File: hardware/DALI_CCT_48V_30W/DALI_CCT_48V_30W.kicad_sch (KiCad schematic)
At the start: 82 parts, among them J1 Phoenix 5.08mm 2-pin 48V_IN, J2 DALI_A/DALI_B Phoenix 5.08mm, J3 LED+/WW-/CW- Phoenix 5.08mm, J4 SWD 1.27mm 4-pin (GND/SWDIO/S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, Q1 AON7534 N-ch 30V 25A, Q2 AON7534 N-ch 30V 25A, Q3 AON6424 N-ch 40V 20A, Q4 AON6424 N-ch 40V 20A

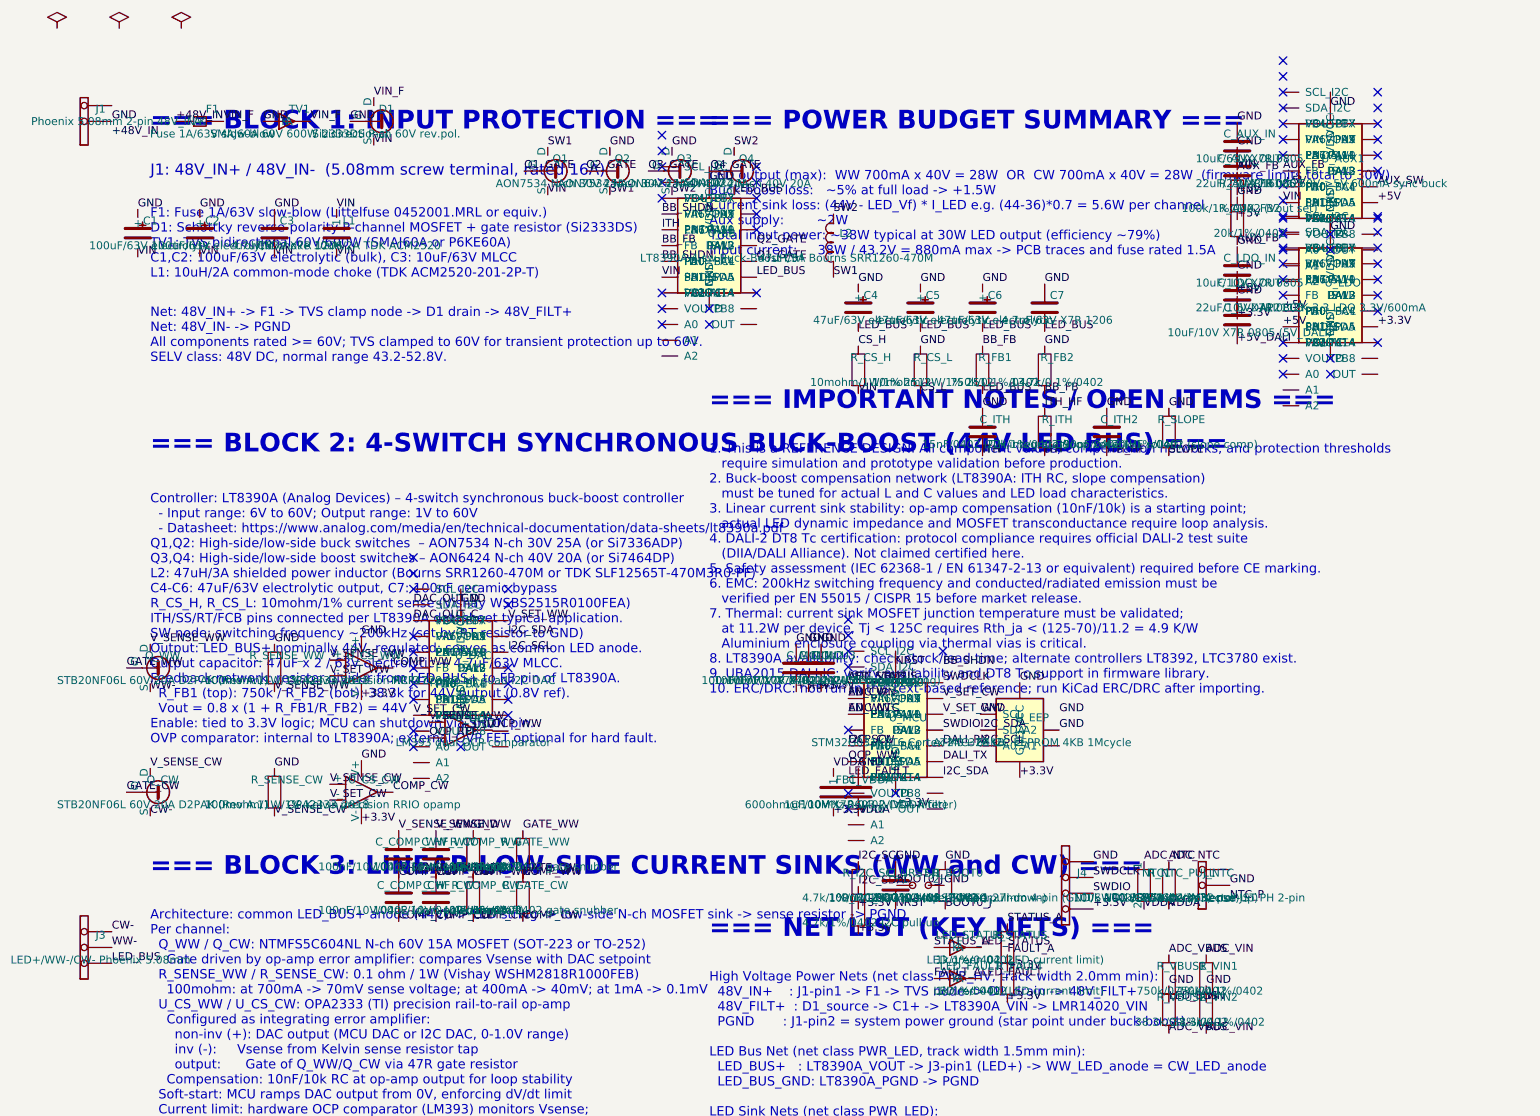
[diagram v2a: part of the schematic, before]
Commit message: Add exact LT8390AIFE KiCad symbol
Co-authored-by: manuelh83 <208121220+manuelh83@users.noreply.github.com>
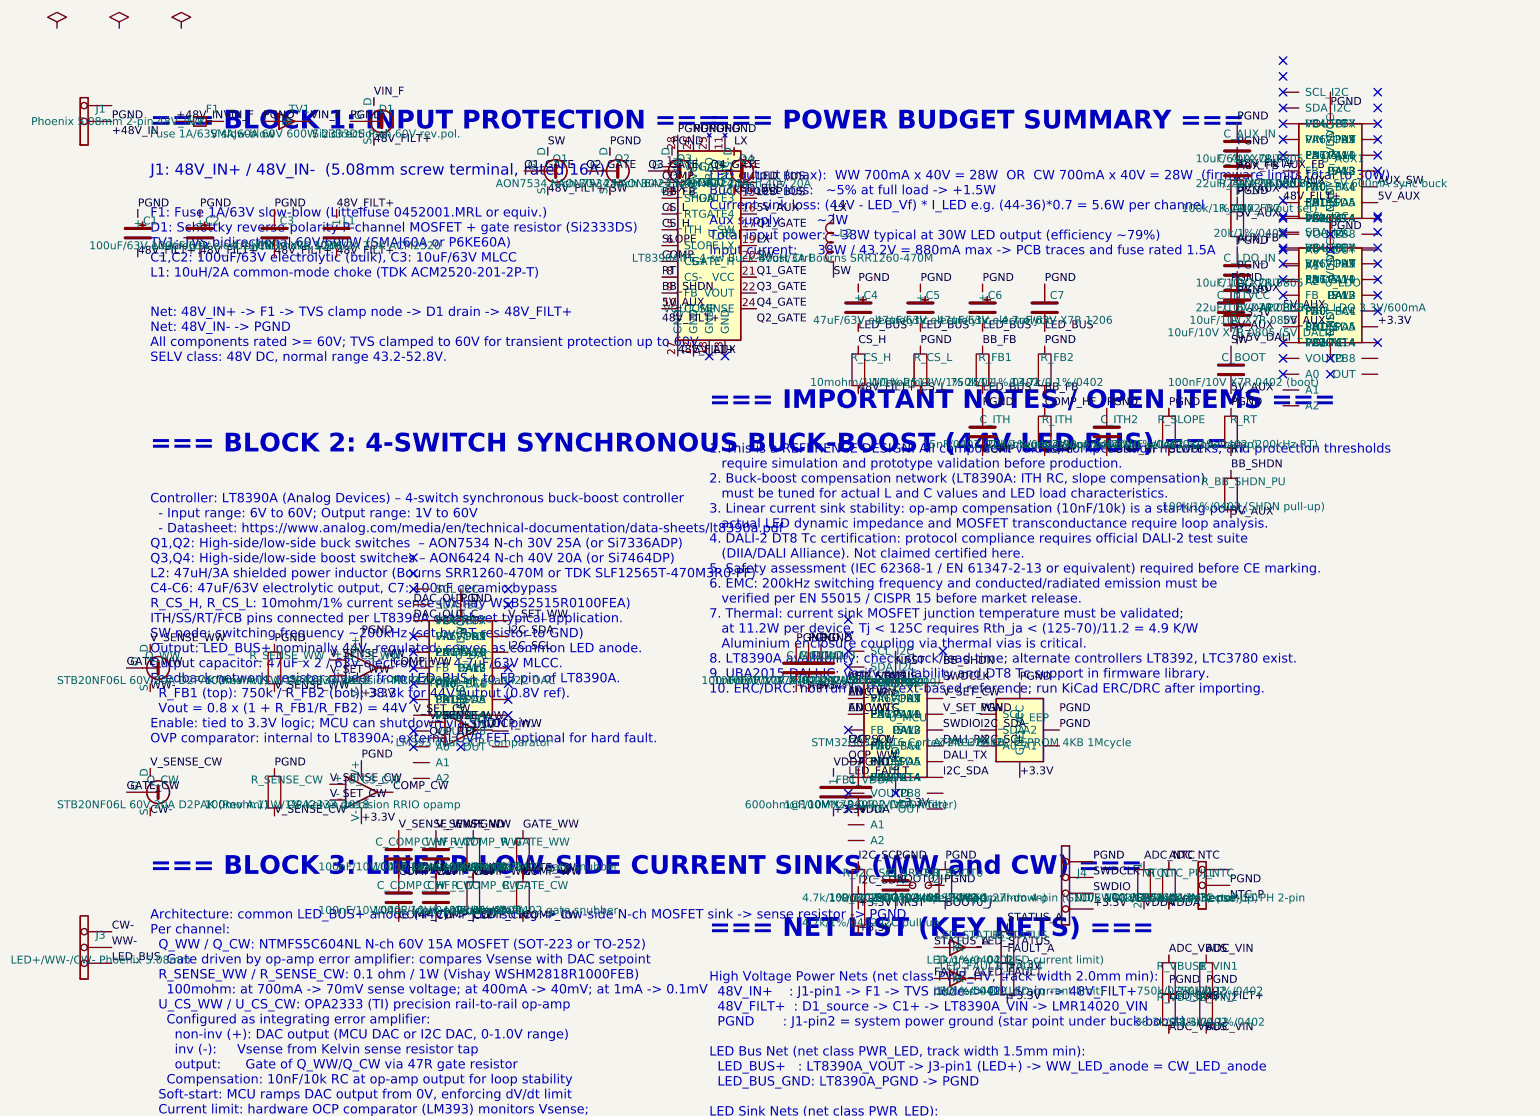
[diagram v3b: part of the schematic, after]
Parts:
- added C_BOOT: 100nF/10V X7R 0402 (boot), Capacitor_SMD:C_0402_1005Metric, symbol Device:C
- added C_INTVCC: 10uF/10V X7R 0805, Capacitor_SMD:C_0805_2012Metric, symbol Device:C
- added R_BB_SHDN_PU: 100k/1%/0402 (SHDN pull-up), Resistor_SMD:R_0402_1005Metric, symbol Device:R
- added R_RT: 470k/1%/0402 (200kHz RT), Resistor_SMD:R_0402_1005Metric, symbol Device:R
- U_BB: value LT8390A 4-sw Buck-Boost Ctrl -> LT8390AIFE 4-sw Buck-Boost Ctrl; symbol Device:IC -> AnalogDevices:LT8390AIFE
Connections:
- net BB_FB: now also U_BB.3 (SHDN); no longer U_BB.FB
- net BB_SHDN: now also U_BB.9 (FB), R_BB_SHDN_PU.1; no longer U_BB.ITH, U_BB.PA0, U_BB.PA6, U_BB.PB0, U_BB.VIN
- net CS_H: now also U_BB.5 (ITH)
- net CS_L: now also U_BB.4 (RT)
- net LED_BUS: now also U_BB.14 (GATE2), U_BB.15 (GATE3); no longer U_BB.PA5, U_BB.SDA
- net Q1_GATE: now also U_BB.17 (SW), U_BB.21 (VCC); no longer U_BB.PA4, U_BB.SCL
- net Q2_GATE: no longer U_BB.DALI-, U_BB.PA13, U_BB.SW2
- net Q3_GATE: now also U_BB.22 (VOUT)
- net Q4_GATE: now also U_BB.24 (VOUT_SENSE)
- net SLOPE: now also U_BB.6 (SLOPE)
- net +5V renamed 5V_AUX
- net 5V_AUX: now also U_BB.10 (COMP), U_BB.12 (GND), U_BB.16 (GATE4), C_BOOT.2, C_INTVCC.2, R_BB_SHDN_PU.2
- net GND renamed PGND
- net PGND: now also U_BB.11 (N.C.), U_BB.25 (FREQ), U_BB.26 (INTVCC), U_BB.28 (VIN), C_INTVCC.1, R_RT.1; no longer U_BB.VDD
- removed net ITH: C_ITH.2, R_ITH.2, U_BB.EN, U_BB.PA7, U_BB.PB6
- net ITH_HF renamed COMP_HF
- net SW1 renamed SW
- net SW: now also U_BB.20 (GATE_H), C_BOOT.1
- net SW2 renamed LX
- net LX: now also U_BB.19 (LX)
- net VIN renamed 48V_FILT+
- net 48V_FILT+: now also U_BB.27 (GND); no longer U_BB.PA1, U_BB.PB1, U_BB.SHDN
- new net COMP: C_ITH.2, R_ITH.2, U_BB.2 (INTVCC), U_BB.7 (CS+)
- new net RT: R_RT.2, U_BB.8 (CS-)
- no-connect marks 101 -> 87

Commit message: Finalize LT8390A exact KiCad symbol update
Co-authored-by: manuelh83 <208121220+manuelh83@users.noreply.github.com>
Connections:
- net 5V_AUX: no longer C_BOOT.2
- net Q1_GATE: no longer U_BB.17 (SW)
- new net GATE_H: C_BOOT.2, U_BB.17 (SW)
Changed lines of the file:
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@@
     (effects (font (size 1.27 1.27)) (justify left bottom))
   )
-  (label "Q1_GATE"
+  (label "GATE_H"
     (at 127.62 47.46 0)
     (fields_autoplaced yes)
@@
     (effects (font (size 1.27 1.27)) (justify left bottom))
   )
-  (label "5V_AUX"
+  (label "GATE_H"
     (at 204 73.81 0)
     (fields_autoplaced yes)

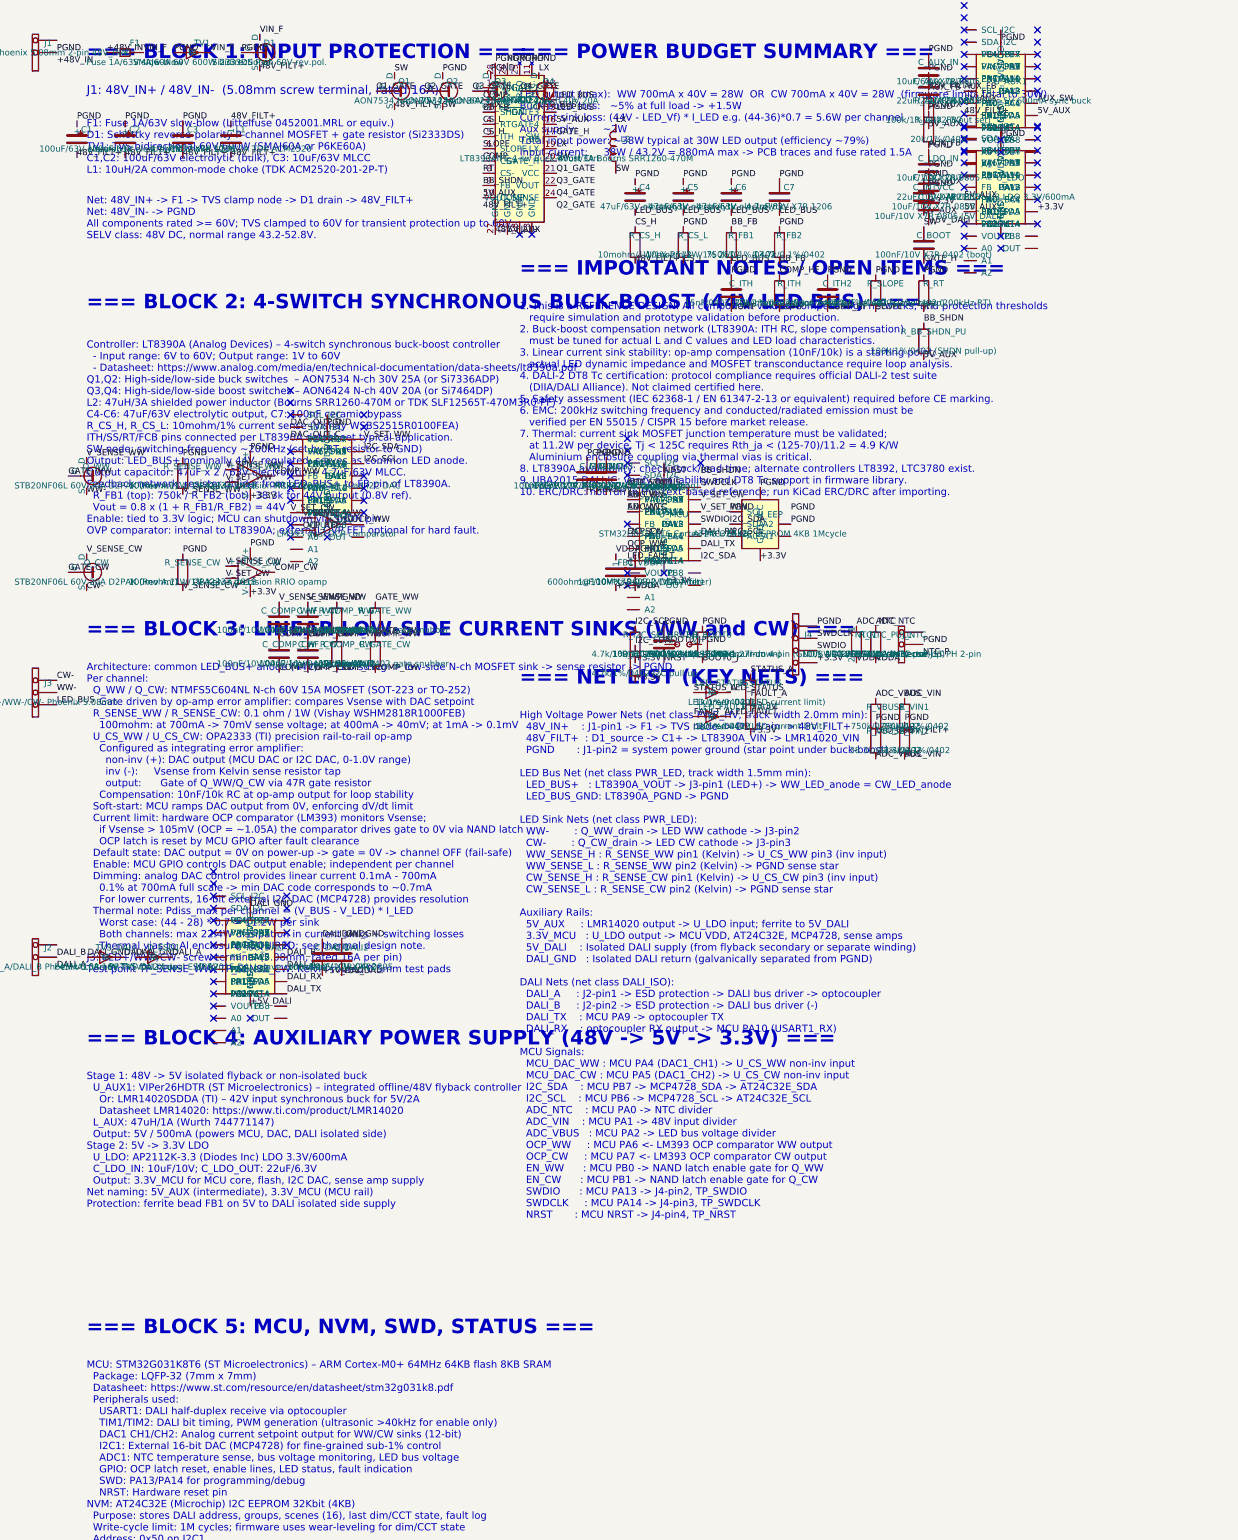
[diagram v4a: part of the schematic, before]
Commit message: fix: correct MCP4728 bit-width (16→12), LMR14020→LMR16006, current limits (700→600mA, 1.05→0.9A), remove adaptive Vbus references
Co-authored-by: manuelh83 <208121220+manuelh83@users.noreply.github.com>
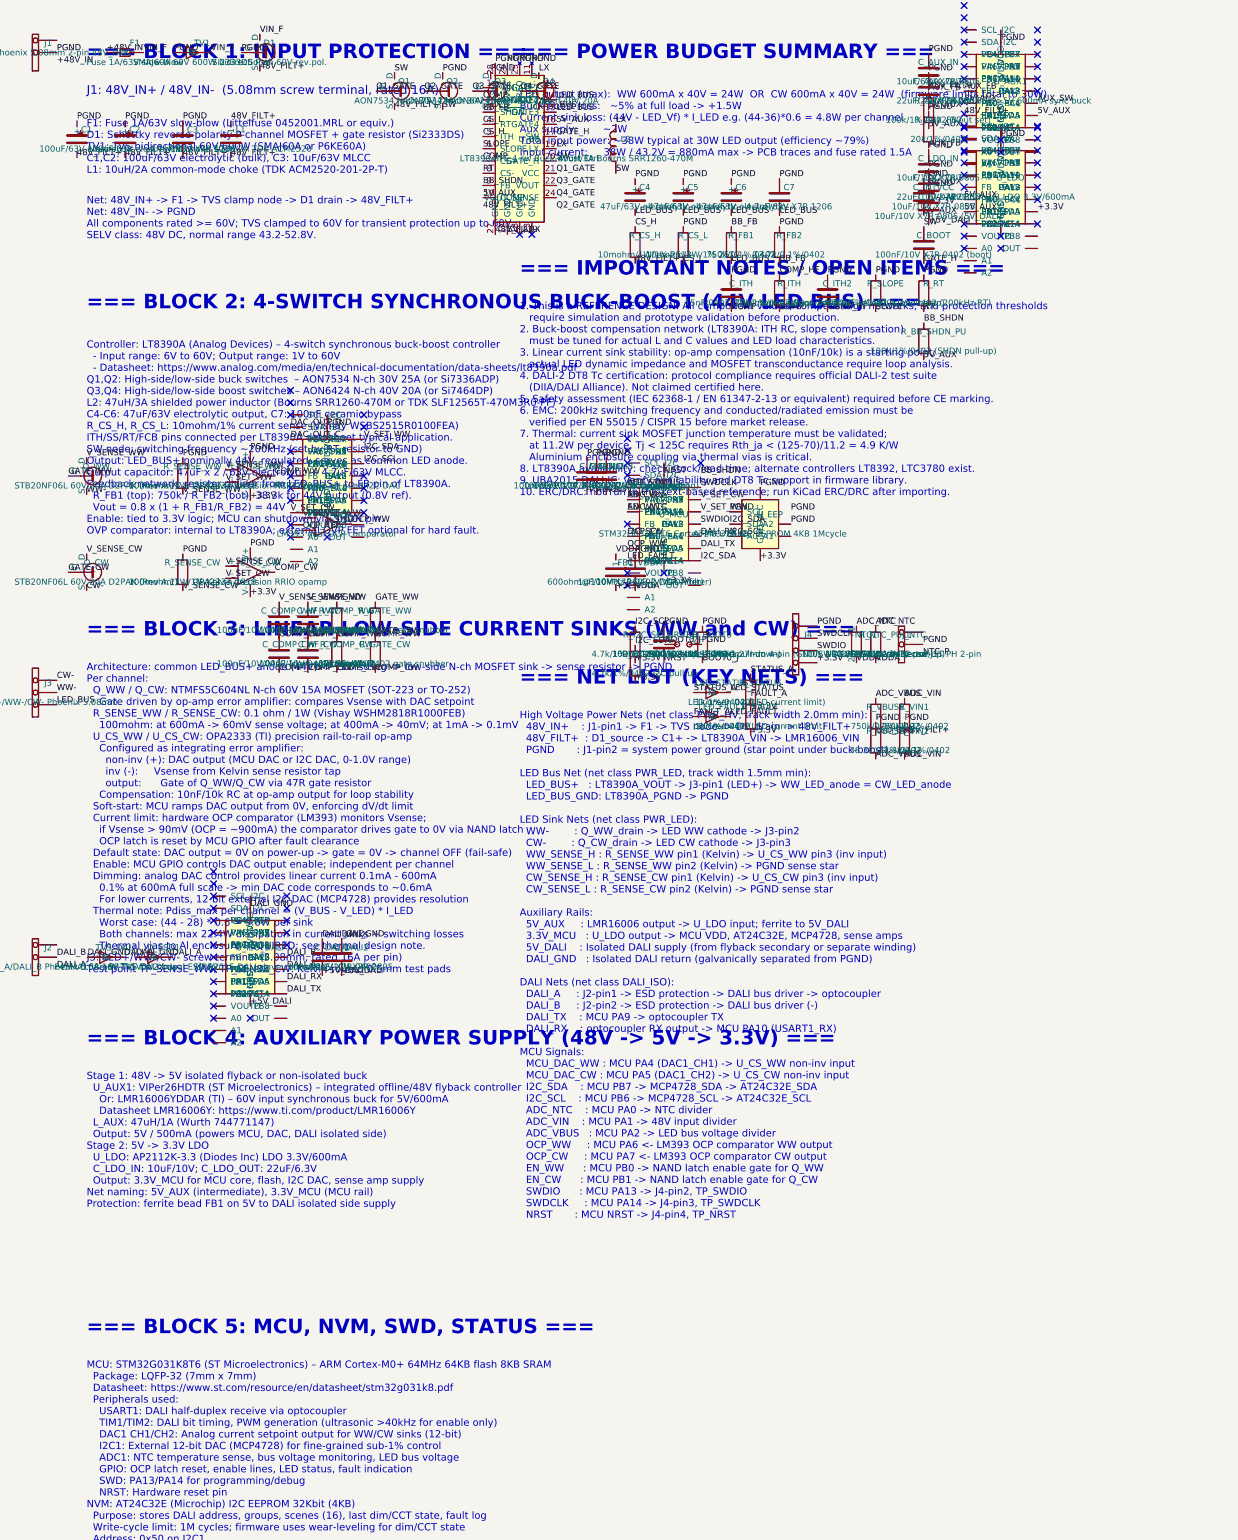
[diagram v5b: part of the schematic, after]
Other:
- note added: "Architecture: common LED_BUS+ anode (44V) -> LED string -> low-side N-ch MOSFET sink -> sense resistor -> PGND Per channel: Q_WW / Q_CW: NTMFS5C604NL N-ch 60V 15A MOSFET (SOT-223 or TO-252) Gate driven by op-amp error amplifier: compares Vsense with DAC setpoint R_SENSE_WW / R_SENSE_CW: 0.1 ohm / 1W (Vishay WSHM2818R1000FEB) 100mohm: at 600mA -> 60mV sense voltage; at 400mA -> 40mV; at 1mA -> 0.1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"
- note added: "High Voltage Power Nets (net class PWR_HV, track width 2.0mm min): 48V_IN+ : J1-pin1 -> F1 -> TVS node -> D1_drain -> 48V_FILT+ 48V_FILT+ : D1_source -> C1+ -> LT8390A_VIN -> LMR16006_VIN PGND : J1-pin2 = system power ground (star point under buck-boost) LED Bus Net (net class PWR_LED, track width 1.5mm min): LED_BUS+ : LT8390A_VOUT -> J3-pin1 (LED+) -> WW_LED_anode = CW_LED_anode LED_BUS_GND: LT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"
- note added: "LED output (max): WW 600mA x 40V = 24W OR CW 600mA x 40V = 24W (firmware limits total to 30W) Buck-boost loss: ~5% at full load -> +1.5W Current sink loss: (44V - LED_Vf) * I_LED e.g. (44-36)*0.6 = 4.8W per channel Aux supply: ~2W Total input power: ~38W typical at 30W LED output (efficiency ~79%) Input current: 38W / 43.2V = 880mA max -> PCB traces and fuse rated 1.5A"
- note added: "Stage 1: 48V -> 5V isolated flyback or non-isolated buck U_AUX1: VIPer26HDTR (ST Microelectronics) – integrated offline/48V flyback controller Or: LMR16006YDDAR (TI) – 60V input synchronous buck for 5V/600mA Datasheet LMR16006Y: https://www.ti.com/product/LMR16006Y L_AUX: 47uH/1A (Wurth 744771147) Output: 5V / 500mA (powers MCU, DAC, DALI isolated side) Stage 2: 5V -> 3.3V LDO U_LDO: AP2112K-3.3 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"
- note removed: "Architecture: common LED_BUS+ anode (44V) -> LED string -> low-side N-ch MOSFET sink -> sense resistor -> PGND Per channel: Q_WW / Q_CW: NTMFS5C604NL N-ch 60V 15A MOSFET (SOT-223 or TO-252) Gate driven by op-amp error amplifier: compares Vsense with DAC setpoint R_SENSE_WW / R_SENSE_CW: 0.1 ohm / 1W (Vishay WSHM2818R1000FEB) 100mohm: at 700mA -> 70mV sense voltage; at 400mA -> 40mV; at 1mA -> 0.1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"
- note removed: "High Voltage Power Nets (net class PWR_HV, track width 2.0mm min): 48V_IN+ : J1-pin1 -> F1 -> TVS node -> D1_drain -> 48V_FILT+ 48V_FILT+ : D1_source -> C1+ -> LT8390A_VIN -> LMR14020_VIN PGND : J1-pin2 = system power ground (star point under buck-boost) LED Bus Net (net class PWR_LED, track width 1.5mm min): LED_BUS+ : LT8390A_VOUT -> J3-pin1 (LED+) -> WW_LED_anode = CW_LED_anode LED_BUS_GND: LT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"
- note removed: "LED output (max): WW 700mA x 40V = 28W OR CW 700mA x 40V = 28W (firmware limits total to 30W) Buck-boost loss: ~5% at full load -> +1.5W Current sink loss: (44V - LED_Vf) * I_LED e.g. (44-36)*0.7 = 5.6W per channel Aux supply: ~2W Total input power: ~38W typical at 30W LED output (efficiency ~79%) Input current: 38W / 43.2V = 880mA max -> PCB traces and fuse rated 1.5A"
- note removed: "Stage 1: 48V -> 5V isolated flyback or non-isolated buck U_AUX1: VIPer26HDTR (ST Microelectronics) – integrated offline/48V flyback controller Or: LMR14020SDDA (TI) – 42V input synchronous buck for 5V/2A Datasheet LMR14020: https://www.ti.com/product/LMR14020 L_AUX: 47uH/1A (Wurth 744771147) Output: 5V / 500mA (powers MCU, DAC, DALI isolated side) Stage 2: 5V -> 3.3V LDO U_LDO: AP2112K-3.3 (Diode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"
